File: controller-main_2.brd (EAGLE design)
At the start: 86 x 58 mm, 18 parts

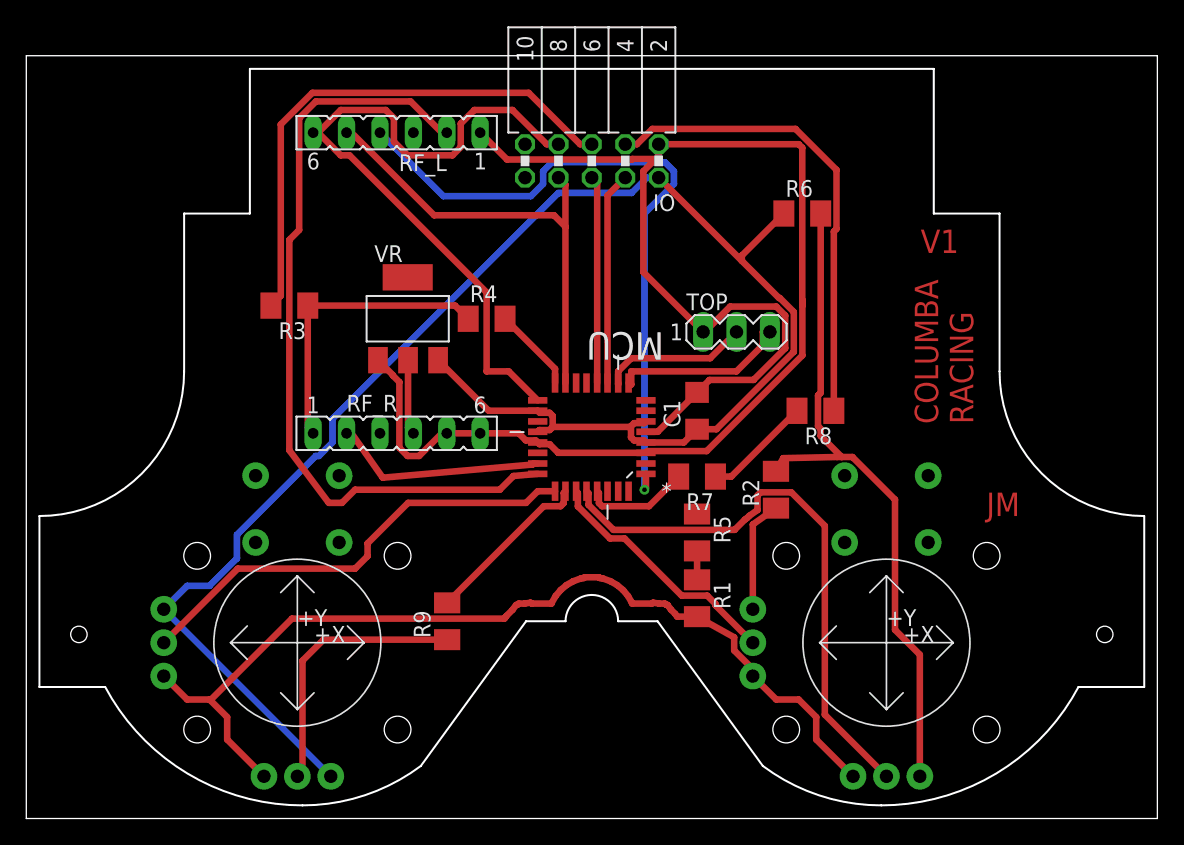
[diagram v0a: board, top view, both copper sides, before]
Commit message: Created V2 main board, updated second board
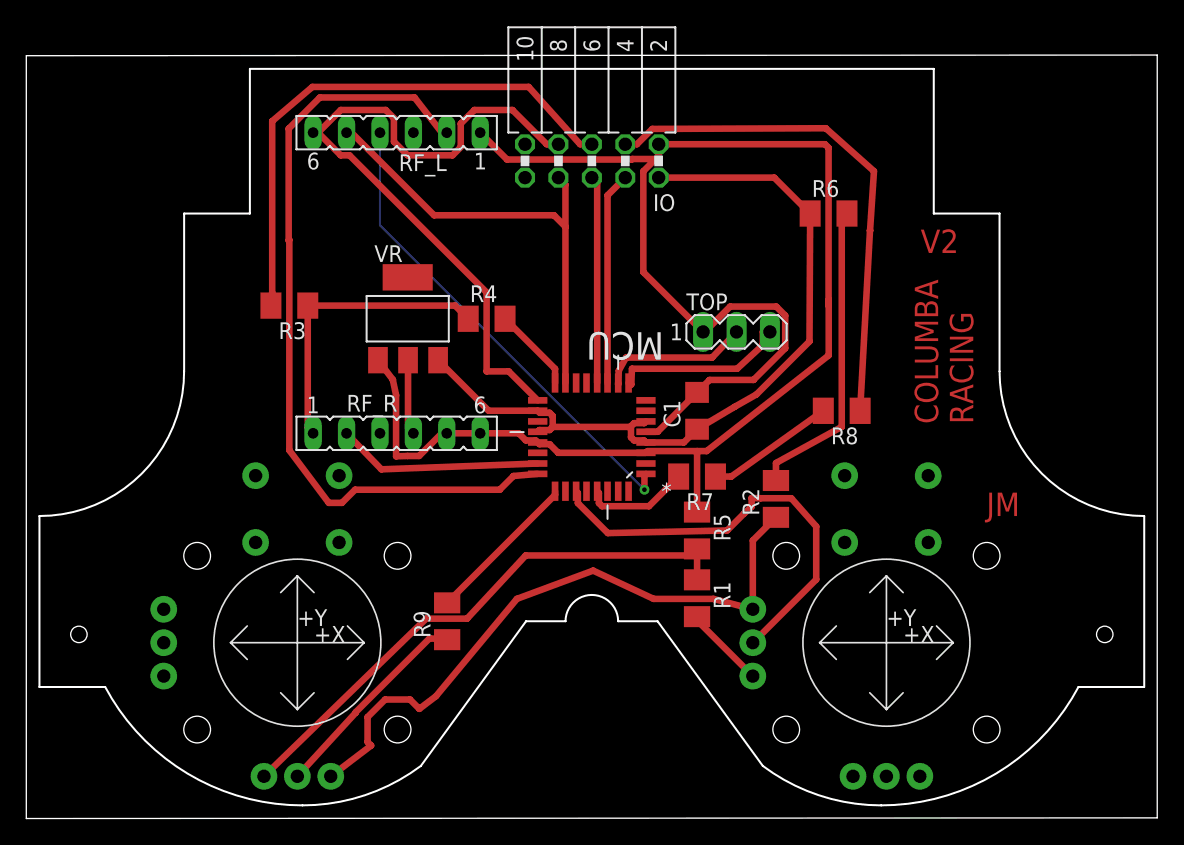
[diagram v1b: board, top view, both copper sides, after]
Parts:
- moved R6 2.00 mm to (61.0, 46.0)
- moved R8 2.00 mm to (62.0, 31.0)
- moved R2 0.70 mm to (57.0, 24.3)
- moved R5 0.15 mm to (51.0, 21.9)
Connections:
- net N$2 renamed LAX2
- removed net GND_R: LAN.GNDX, LAN.GNDY, R1.2, RAN.GNDX, RAN.GNDY
- removed net LAY: LAN.OUTY, MCU.25
- removed net RAX: MCU.28, RAN.OUTX
- new net GND2: LAN.GNDX, R1.1, R5.2
- net 5V: no longer LAN.VCCX, LAN.VCCY
- net 5V2: no longer RAN.VCCX
- net 5V_R: now also LAN.VCCX
- net LAX: now also MCU.25; no longer MCU.26
- net N$1: now also R1.2, RAN.GNDY; no longer R1.1, R5.2
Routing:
- net GND_R: track 72.6 -> 0.00 mm
- net 5V: track 129.8 -> 59.6 mm
- net RAX: track 43.7 -> 0.00 mm
- net GND2: track 0.00 -> 42.2 mm
- net 5V_R: track 8.60 -> 48.8 mm
- net LAY: track 35.1 -> 0.00 mm
- net 5V2: track 52.1 -> 23.4 mm
- net RF_INT: track 52.7 -> 36.7 mm
- net RAY: track 18.9 -> 33.3 mm
- net GND: track 123.8 -> 132.3 mm
- net LAX2: track 20.6 -> 15.9 mm
- net N$1: track 2.20 -> 6.28 mm
- net RST3: track 36.2 -> 39.0 mm
- net RST2: track 8.27 -> 9.80 mm
- net LAX: track 13.0 -> 11.9 mm
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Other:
- board text added: "V2"
- board text removed: "V1"

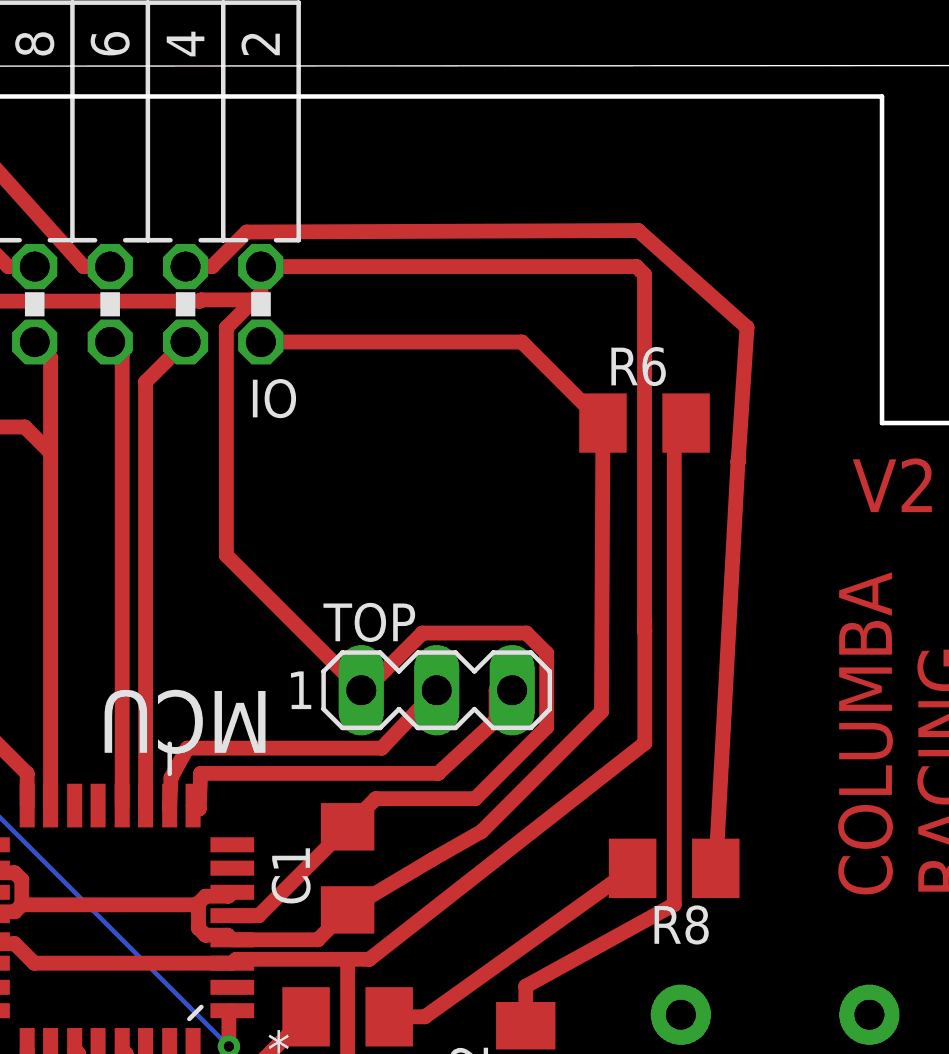
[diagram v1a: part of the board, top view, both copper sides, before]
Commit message: Moved reset trace
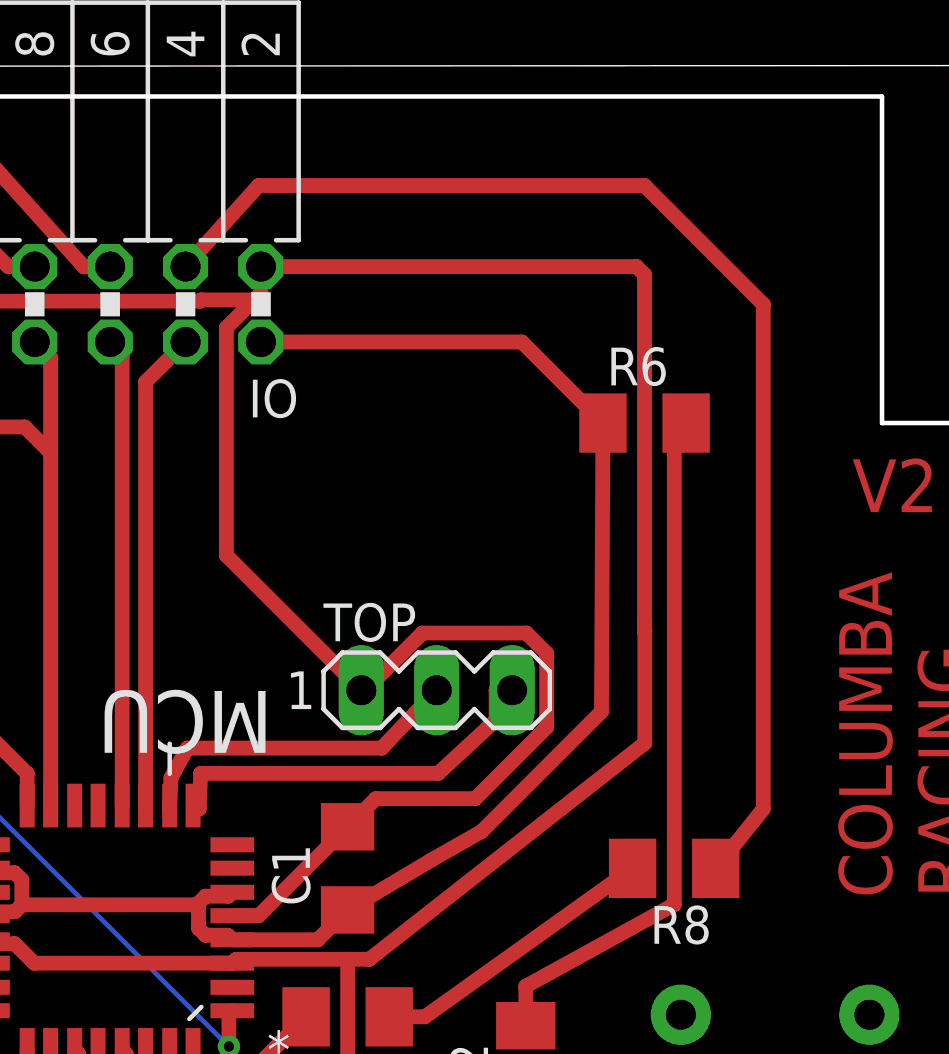
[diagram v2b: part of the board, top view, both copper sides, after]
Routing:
- net RST3: track 39.0 -> 41.9 mm
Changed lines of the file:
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@@
 <contactref element="IO" pad="4"/>
 <contactref element="R8" pad="1"/>
-<wire x1="64.1524" y1="44.68331875" x2="64.15" y2="44.73091875" width="0.5" layer="1"/>
-<wire x1="64.15" y1="44.73091875" x2="63.4" y2="31" width="0.5" layer="1"/>
-<wire x1="45.54" y1="51.27" x2="46.4332875" y2="51.27" width="0.5" layer="1"/>
-<wire x1="46.4332875" y1="51.27" x2="47.5976875" y2="52.4344" width="0.5" layer="1"/>
-<wire x1="47.5976875" y1="52.4344" x2="60.7882375" y2="52.4844" width="0.5" layer="1"/>
-<wire x1="60.7882375" y1="52.4844" x2="64.4524" y2="49.2202375" width="0.5" layer="1"/>
-<wire x1="64.4524" y1="49.2202375" x2="64.1524" y2="44.68331875" width="0.5" layer="1"/>
+<wire x1="45.54" y1="51.27" x2="48" y2="54" width="0.5" layer="1"/>
+<wire x1="48" y1="54" x2="61" y2="54" width="0.5" layer="1"/>
+<wire x1="61" y1="54" x2="65" y2="50" width="0.5" layer="1"/>
+<wire x1="65" y1="50" x2="65" y2="33" width="0.5" layer="1"/>
+<wire x1="65" y1="33" x2="63.4" y2="31" width="0.5" layer="1"/>
 </signal>
 <signal name="RST2">
